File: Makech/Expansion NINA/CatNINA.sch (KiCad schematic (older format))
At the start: 7 parts, among them J1 Expansion, U1 ESP32-WROOM

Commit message: Init PCB and netlist
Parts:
- J1: footprint (none) -> Pines:61301221121
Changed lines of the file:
@@
 F 0 "J1" H 9105 2147 50  0000 C CNN
 F 1 "Expansion" H 9105 2056 50  0000 C CNN
-F 2 "" H 9055 1730 50  0001 C CNN
+F 2 "Pines:61301221121" H 9055 1730 50  0001 C CNN
 F 3 "~" H 9055 1730 50  0001 C CNN
 	1    9055 1730

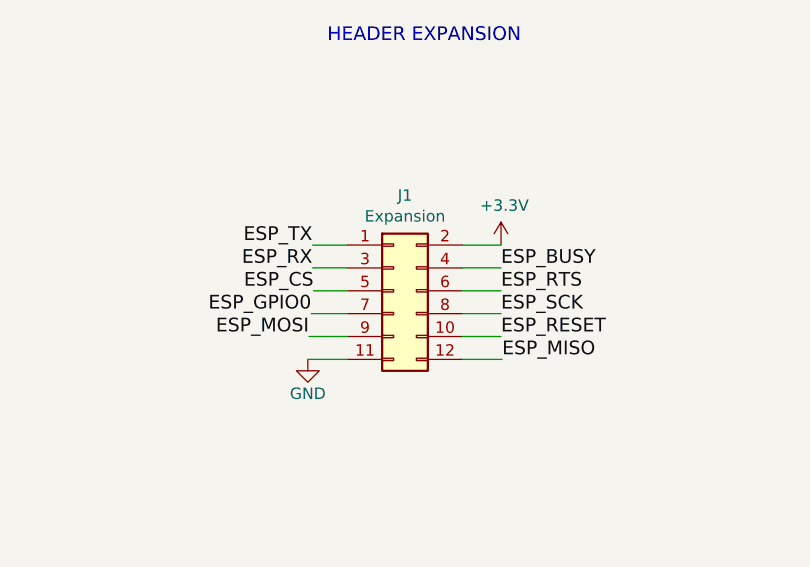
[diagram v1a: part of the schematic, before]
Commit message: update schematic
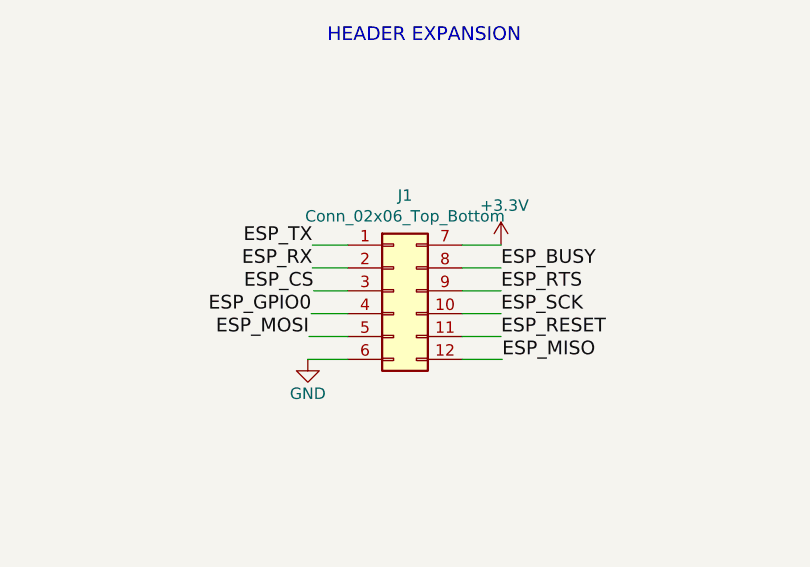
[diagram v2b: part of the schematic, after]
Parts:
- removed J1: Expansion, Pines:61301221121, symbol Connector_Generic:Conn_02x06_Odd_Even
- added J1: Conn_02x06_Top_Bottom, Pines:61301221121, symbol Connector_Generic:Conn_02x06_Top_Bottom
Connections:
- net +3V3: now also J1.7 (Pin_7)
- net ESP_BUSY: now also J1.8 (Pin_8)
- net ESP_CS: now also J1.3 (Pin_3)
- net ESP_GPIO0: now also J1.4 (Pin_4)
- net ESP_MISO: now also J1.12 (Pin_12)
- net ESP_MOSI: now also J1.5 (Pin_5)
- net ESP_RESET: now also J1.11 (Pin_11)
- net ESP_RTS: now also J1.9 (Pin_9)
- net ESP_RX: now also J1.2 (Pin_2)
- net ESP_SCK: now also J1.10 (Pin_10)
- net ESP_TX: now also J1.1 (Pin_1)
- net GND: now also J1.6 (Pin_6)
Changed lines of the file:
@@
 Text Label 9525 1830 0    60   ~ 0
 ESP_SCK
-$Comp
-L Connector_Generic:Conn_02x06_Odd_Even J1
-U 1 1 5CEE89FD
-P 9055 1730
-F 0 "J1" H 9105 2147 50  0000 C CNN
-F 1 "Expansion" H 9105 2056 50  0000 C CNN
-F 2 "Pines:61301221121" H 9055 1730 50  0001 C CNN
-F 3 "~" H 9055 1730 50  0001 C CNN
-	1    9055 1730
-	1    0    0    -1
-$EndComp
 Wire Wire Line
 	9355 1530 9525 1530
@@
 	1    0    0    -1
 $EndComp
+$Comp
+L Connector_Generic:Conn_02x06_Top_Bottom J1
+U 1 1 5CF127AA
+P 9055 1730
+F 0 "J1" H 9105 2147 50  0000 C CNN
+F 1 "Conn_02x06_Top_Bottom" H 9105 2056 50  0000 C CNN
+F 2 "Pines:61301221121" H 9055 1730 50  0001 C CNN
+F 3 "~" H 9055 1730 50  0001 C CNN
+	1    9055 1730
+	1    0    0    -1
+$EndComp

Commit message: add man # to connector
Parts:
- J1: manf # (none) -> 61000621121
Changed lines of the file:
@@
 F 2 "Pines:61301221121" H 9055 1730 50  0001 C CNN
 F 3 "~" H 9055 1730 50  0001 C CNN
+F 4 "61000621121" H 9055 1730 50  0001 C CNN "manf #"
 	1    9055 1730
 	1    0    0    -1

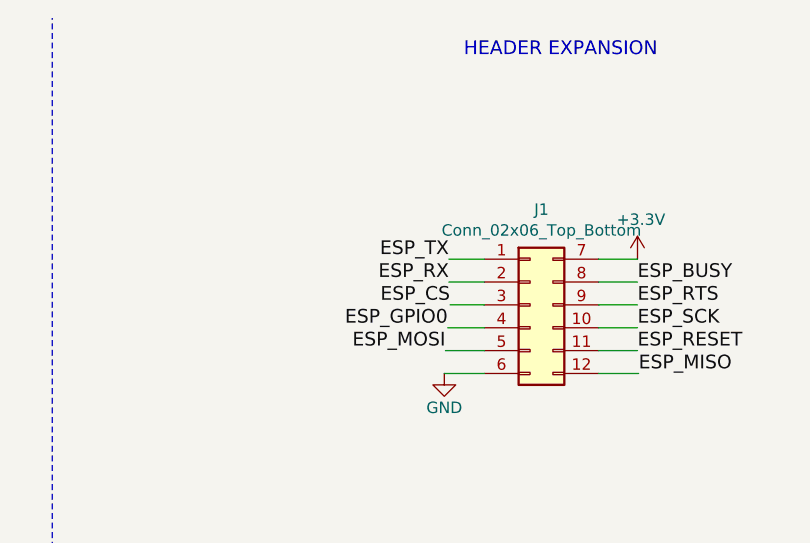
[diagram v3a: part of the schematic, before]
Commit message: move conector
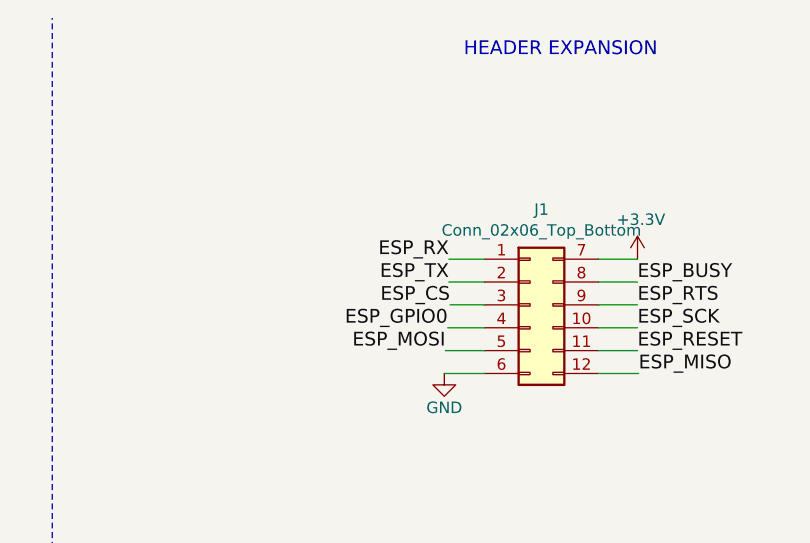
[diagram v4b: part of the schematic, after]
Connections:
- net ESP_RX: now also J1.1 (Pin_1); no longer J1.2 (Pin_2)
- net ESP_TX: now also J1.2 (Pin_2); no longer J1.1 (Pin_1)
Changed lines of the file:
@@
 Text Label 9530 2030 0    60   ~ 0
 ESP_MISO
+Text Label 8700 1530 2    60   ~ 0
+ESP_RX
 Text Label 8700 1630 2    60   ~ 0
-ESP_RX
-Text Label 8700 1530 2    60   ~ 0
 ESP_TX
 Text Label 9525 1730 0    60   ~ 0

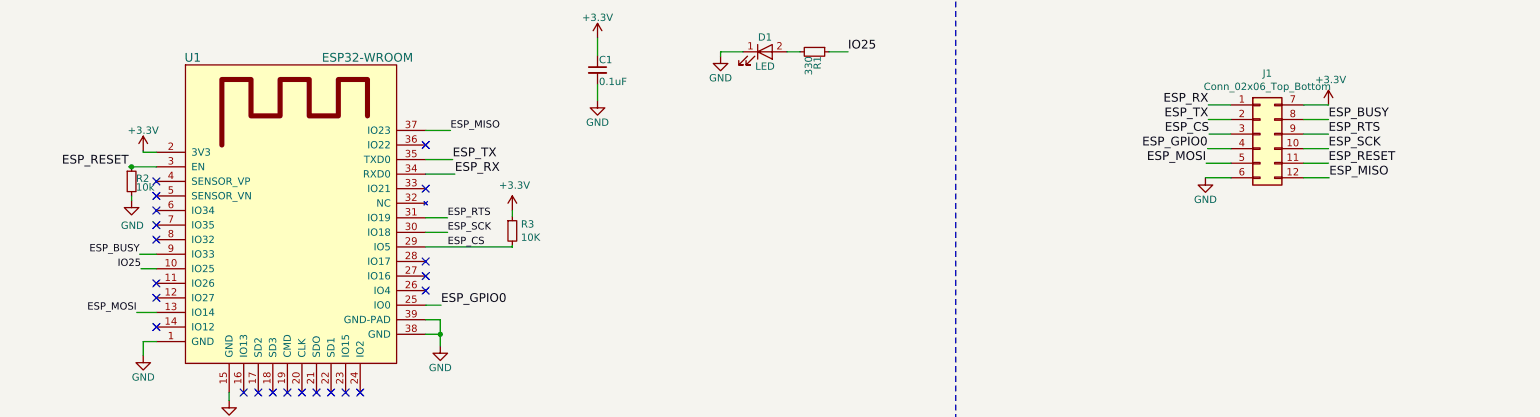
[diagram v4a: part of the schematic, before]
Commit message: init cat nina support BLE
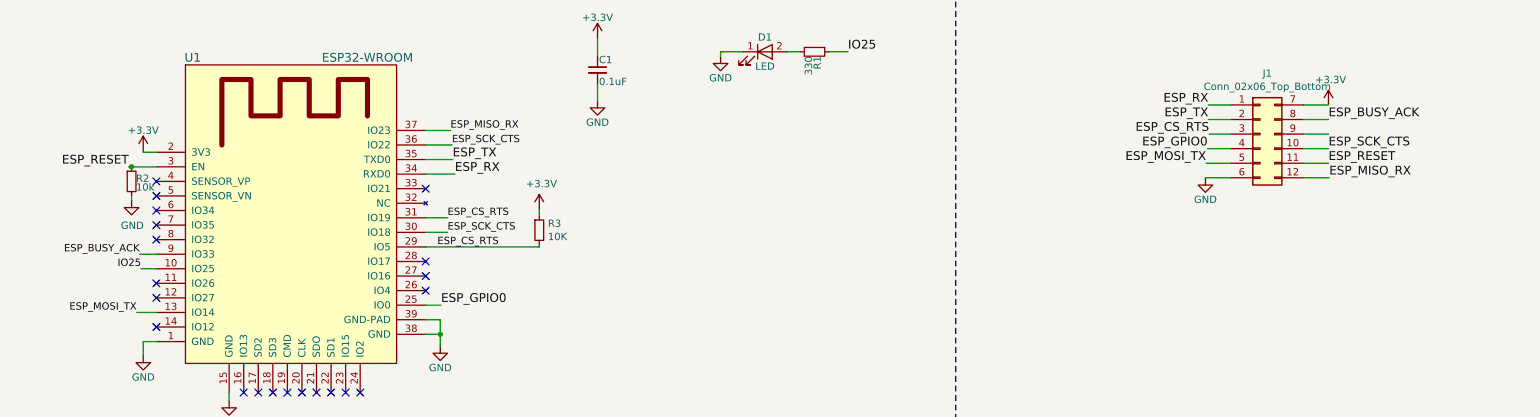
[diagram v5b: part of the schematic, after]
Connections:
- net ESP_SCK is gone; now on net ESP_SCK_CTS: J1.10 (Pin_10), U1.30 (IO18)
- net ESP_SCK_CTS: now reaches U1.36 (IO22)
- net ESP_BUSY renamed ESP_BUSY_ACK
- net ESP_CS renamed ESP_CS_RTS
- net ESP_CS_RTS: now also U1.31 (IO19)
- net ESP_MISO renamed ESP_MISO_RX
- net ESP_MOSI renamed ESP_MOSI_TX
- net ESP_RTS: no longer names the net of J1.9 (Pin_9)
- net ESP_RTS: no longer U1.31 (IO19)
- no-connect marks 22 -> 21
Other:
- moved on the sheet: R3
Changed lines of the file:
@@
 EESchema Schematic File Version 4
 LIBS:CatNINA-cache
-EELAYER 29 0
+EELAYER 30 0
 EELAYER END
 $Descr A4 11693 8268
@@
 Sheet 1 1
 Title "CatNINA"
-Date "2019-05-28"
-Rev "0.1"
+Date "2019-10-19"
+Rev "0.2"
 Comp "Electronic Cats"
 Comment1 ""
@@
 ESP_TX
 NoConn ~ 1475 2255
-NoConn ~ 3325 1805
 NoConn ~ 3325 2105
 NoConn ~ 3325 2705
@@
 ESP_RESET
 Text Label 8685 1930 2    60   ~ 0
-ESP_MOSI
+ESP_MOSI_TX
 Text Label 9530 2030 0    60   ~ 0
-ESP_MISO
+ESP_MISO_RX
 Text Label 8700 1530 2    60   ~ 0
 ESP_RX
 Text Label 8700 1630 2    60   ~ 0
 ESP_TX
-Text Label 9525 1730 0    60   ~ 0
-ESP_RTS
 Text Label 8695 1830 2    60   ~ 0
 ESP_GPIO0
 Text Label 8705 1730 2    60   ~ 0
-ESP_CS
+ESP_CS_RTS
 $Comp
 L CatNINA-rescue:GND-power1-BLE_WIFI_HID-rescue-BLE_WIFI_HID-rescue #PWR06
@@
 	3325 2405 3475 2405
 Text Label 3475 2305 0    50   ~ 0
-ESP_RTS
+ESP_CS_RTS
 Text Label 3475 2405 0    50   ~ 0
-ESP_SCK
-Text Label 3475 2505 0    50   ~ 0
-ESP_CS
+ESP_SCK_CTS
+Text Label 3405 2505 0    50   ~ 0
+ESP_CS_RTS
 Wire Wire Line
 	1475 2955 1340 2955
@@
 	1475 2555 1360 2555
 Text Label 1340 2955 2    50   ~ 0
-ESP_MOSI
+ESP_MOSI_TX
 Text Label 1360 2555 2    50   ~ 0
-ESP_BUSY
+ESP_BUSY_ACK
 NoConn ~ 1475 2355
 Wire Wire Line
 	3325 1705 3495 1705
 Text Label 3495 1705 0    50   ~ 0
-ESP_MISO
+ESP_MISO_RX
 $Comp
 L power:GND #PWR07
@@
 Wire Wire Line
 	1305 2155 1305 2185
-Wire Wire Line
-	3920 2505 3920 2495
-Wire Wire Line
-	3325 2505 3920 2505
 $Comp
 L Device:R_Small R3
 U 1 1 5C941D1D
-P 3920 2395
-F 0 "R3" H 3979 2441 50  0000 L CNN
-F 1 "10K" H 3979 2350 50  0000 L CNN
-F 2 "Resistors_SMD:R_0805_HandSoldering" H 3920 2395 50  0001 C CNN
-F 3 "~" H 3920 2395 50  0001 C CNN
-	1    3920 2395
-	1    0    0    -1
-$EndComp
-Wire Wire Line
-	3920 2295 3920 2255
+P 4105 2390
+F 0 "R3" H 4164 2436 50  0000 L CNN
+F 1 "10K" H 4164 2345 50  0000 L CNN
+F 2 "Resistors_SMD:R_0805_HandSoldering" H 4105 2390 50  0001 C CNN
+F 3 "~" H 4105 2390 50  0001 C CNN
+	1    4105 2390
+	1    0    0    -1
+$EndComp
 $Comp
 L power:+3.3V #PWR08
 U 1 1 5C9443CD
-P 3920 2255
-F 0 "#PWR08" H 3920 2105 50  0001 C CNN
-F 1 "+3.3V" H 3935 2428 50  0000 C CNN
-F 2 "" H 3920 2255 50  0001 C CNN
-F 3 "" H 3920 2255 50  0001 C CNN
-	1    3920 2255
+P 4105 2245
+F 0 "#PWR08" H 4105 2095 50  0001 C CNN
+F 1 "+3.3V" H 4120 2418 50  0000 C CNN
+F 2 "" H 4105 2245 50  0001 C CNN
+F 3 "" H 4105 2245 50  0001 C CNN
+	1    4105 2245
 	1    0    0    -1
 $EndComp
@@
 	11195 4080 11195 4100
 Text Label 9525 1630 0    60   ~ 0
-ESP_BUSY
+ESP_BUSY_ACK
 Text Label 9525 1830 0    60   ~ 0
-ESP_SCK
+ESP_SCK_CTS
 Wire Wire Line
 	9355 1530 9525 1530
@@
 	1    0    0    -1
 $EndComp
+Wire Wire Line
+	4105 2505 4105 2490
+Wire Wire Line
+	3325 2505 4105 2505
+Wire Wire Line
+	4105 2290 4105 2245
+Wire Wire Line
+	3325 1805 3505 1805
+Text Label 3505 1805 0    50   ~ 0
+ESP_SCK_CTS
 $EndSCHEMATC

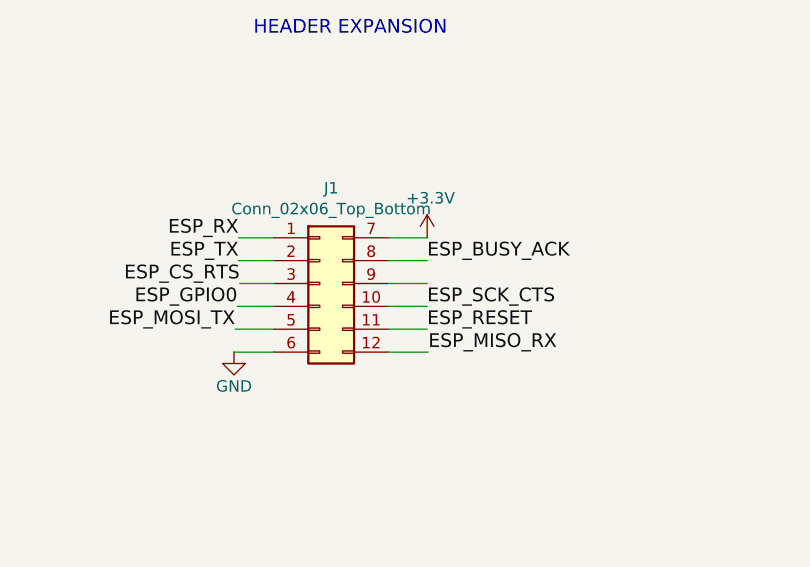
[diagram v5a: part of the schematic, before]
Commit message: remove not connect lines
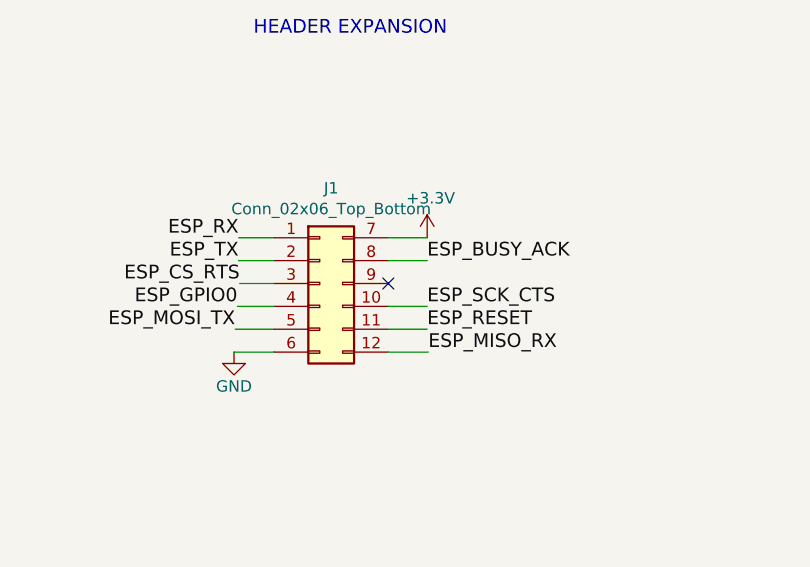
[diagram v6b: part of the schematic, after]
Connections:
- no-connect marks 21 -> 22
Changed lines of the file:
@@
 	9355 1630 9525 1630
-Wire Wire Line
-	9355 1730 9525 1730
 Wire Wire Line
 	9355 1830 9525 1830
@@
 Text Label 3505 1805 0    50   ~ 0
 ESP_SCK_CTS
+NoConn ~ 9355 1730
 $EndSCHEMATC
